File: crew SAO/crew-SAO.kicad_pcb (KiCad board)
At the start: 2 copper layers, 78.8 x 16.5 mm, 3 parts

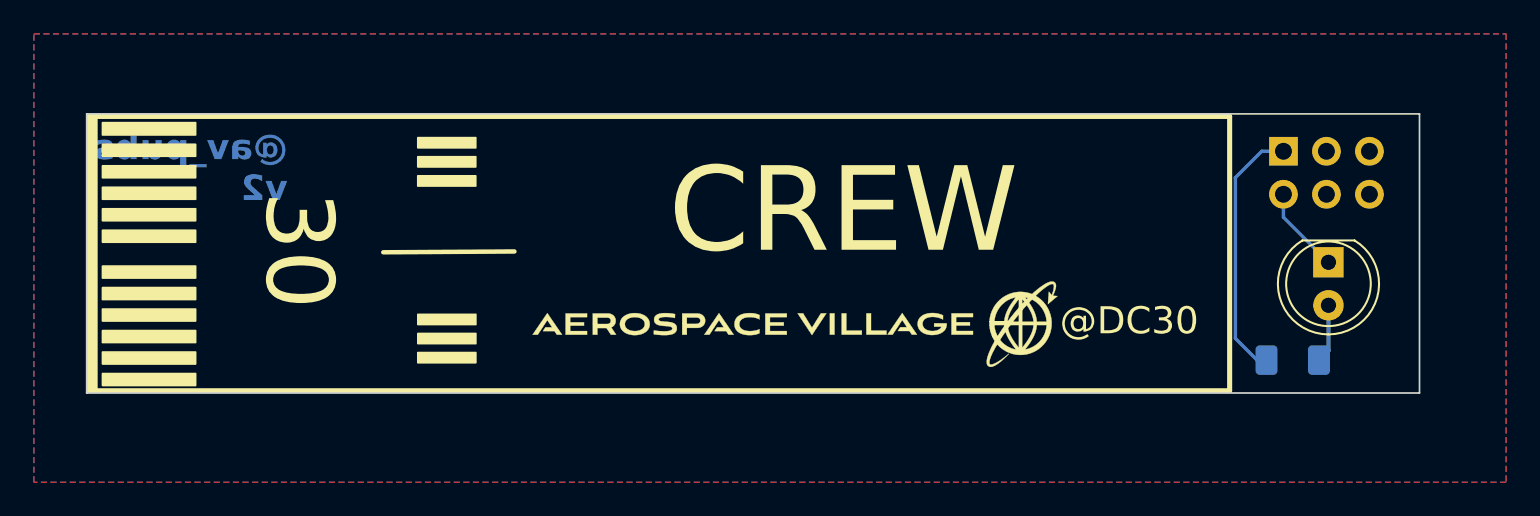
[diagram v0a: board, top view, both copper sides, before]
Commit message: speaker and crew SAOs updated to v3 that moves the connector slightly so it doesn't stick out
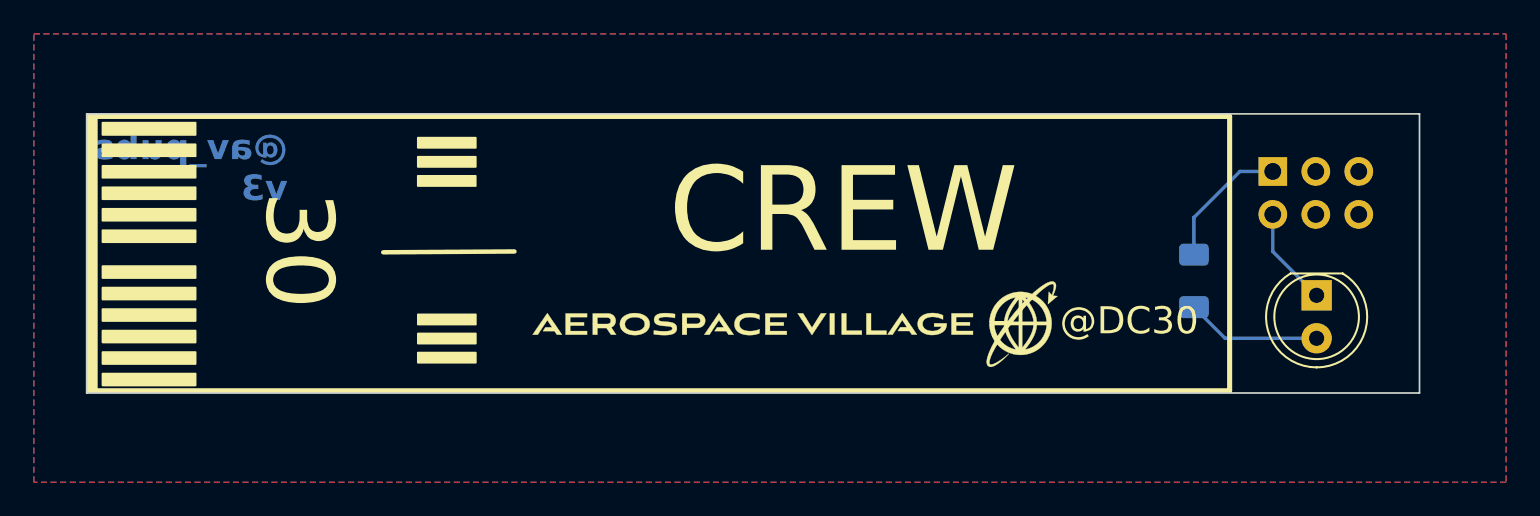
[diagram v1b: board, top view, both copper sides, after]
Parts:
- moved REF** 7.48 mm to (149.6, 132.6), turned to -90 degrees
- moved REF** 2.07 mm to (156.8, 133.4)
- moved REF** 1.35 mm to (154.2, 126.1)
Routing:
- net (no net): track 24.0 -> 21.9 mm
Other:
- board text added: "@av_pubs v3"
- board text removed: "@av_pubs v2"
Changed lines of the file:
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@@
   (net 0 "")
   (footprint "LED_THT:LED_D5.0mm" (layer "F.Cu")
-    (at 157.5 131.5 -90)
+    (at 156.8 133.45 -90)
     (descr "LED, diameter 5.0mm, 2 pins, http://cdn-reichelt.de/documents/datenblatt/A500/LL-504BC2E-009.pdf")
     (tags "LED diameter 5.0mm 2 pins")
@@
   )
   (footprint "Connector_PinHeader_2.54mm:PinHeader_2x03_P2.54mm_Vertical" (layer "B.Cu")
-    (at 154.84 124.94 -90)
+    (at 154.21 126.13 -90)
     (descr "Through hole straight pin header, 2x03, 2.54mm pitch, double rows")
     (tags "Through hole pin header THT 2x03 2.54mm double row")
@@
   )
   (footprint "Resistor_SMD:R_1206_3216Metric_Pad1.30x1.75mm_HandSolder" (layer "B.Cu")
-    (at 155.39 137.28 180)
+    (at 149.55 132.6 -90)
     (descr "Resistor SMD 1206 (3216 Metric), square (rectangular) end terminal, IPC_7351 nominal with elongated pad for handsoldering. (Body size source: IPC-SM-782 page 72, https://www.pcb-3d.com/wordpress/wp-content/uploads/ipc-sm-782a_amendment_1_and_2.pdf), generated with kicad-footprint-generator")
     (tags "resistor handsolder")
     (attr smd)
-    (fp_text reference "REF**" (at 0 1.82) (layer "B.SilkS") hide
+    (fp_text reference "REF**" (at 0 1.82 -270) (layer "B.SilkS") hide
         (effects (font (size 1 1) (thickness 0.15)) (justify mirror))
     )
-    (fp_text value "R_1206_3216Metric_Pad1.30x1.75mm_HandSolder" (at 0 -1.82) (layer "B.Fab")
+    (fp_text value "R_1206_3216Metric_Pad1.30x1.75mm_HandSolder" (at 0 -1.82 -270) (layer "B.Fab")
         (effects (font (size 1 1) (thickness 0.15)) (justify mirror))
     )
-    (fp_text user "${REFERENCE}" (at 0 0) (layer "B.Fab")
+    (fp_text user "${REFERENCE}" (at 0 0 -270) (layer "B.Fab")
         (effects (font (size 0.8 0.8) (thickness 0.12)) (justify mirror))
     )
@@
     (fp_line (start 1.6 0.8) (end 1.6 -0.8)
       (stroke (width 0.1) (type solid)) (layer "B.Fab"))
-    (pad "1" smd roundrect (at -1.55 0 180) (size 1.3 1.75) (layers "B.Cu" "B.Paste" "B.Mask") (roundrect_rratio 0.1923076923))
-    (pad "2" smd roundrect (at 1.55 0 180) (size 1.3 1.75) (layers "B.Cu" "B.Paste" "B.Mask") (roundrect_rratio 0.1923076923))
+    (pad "1" smd roundrect (at -1.55 0 270) (size 1.3 1.75) (layers "B.Cu" "B.Paste" "B.Mask") (roundrect_rratio 0.1923076923))
+    (pad "2" smd roundrect (at 1.55 0 270) (size 1.3 1.75) (layers "B.Cu" "B.Paste" "B.Mask") (roundrect_rratio 0.1923076923))
     (model "${KICAD6_3DMODEL_DIR}/Resistor_SMD.3dshapes/R_1206_3216Metric.wrl"
       (offset (xyz 0 0 0))
@@
   (gr_rect (start 84.12 122.73) (end 162.88 139.22)
     (stroke (width 0.1) (type default)) (fill none) (layer "Edge.Cuts"))
-  (gr_text "@av_pubs\nv2" (at 96 128) (layer "B.Cu")
+  (gr_text "@av_pubs\nv3" (at 96 128) (layer "B.Cu")
     (effects (font (size 1.5 1.5) (thickness 0.3) bold) (justify left bottom mirror))
   )
-  (gr_text "jlcjlcjlcjlc" (at 91 137.5) (layer "B.SilkS")
-    (effects (font (size 1.5 1.5) (thickness 0.3) bold) (justify mirror))
+  (gr_text "jlcjlcjlcjlc" (at 92.45 138.65) (layer "B.SilkS")
+    (effects (font (size 1 1) (thickness 0.15)) (justify left bottom mirror))
   )
   (gr_text "30" (at 94.3 127.29 -90) (layer "F.SilkS")
@@
     )
   )
-  (segment (start 152 126.5) (end 152 136) (width 0.2) (layer "B.Cu") (net 0))
-  (segment (start 153.28 137.28) (end 153.84 137.28) (width 0.2) (layer "B.Cu") (net 0))
-  (segment (start 157.5 134.04) (end 157.5 136.72) (width 0.25) (layer "B.Cu") (net 0))
-  (segment (start 154.84 124.94) (end 153.56 124.94) (width 0.2) (layer "B.Cu") (net 0))
-  (segment (start 154.84 127.48) (end 154.84 128.84) (width 0.2) (layer "B.Cu") (net 0))
-  (segment (start 153.56 124.94) (end 152 126.5) (width 0.2) (layer "B.Cu") (net 0))
-  (segment (start 154.84 128.84) (end 157.5 131.5) (width 0.2) (layer "B.Cu") (net 0))
-  (segment (start 152 136) (end 153.28 137.28) (width 0.2) (layer "B.Cu") (net 0))
-  (segment (start 157.5 136.72) (end 156.94 137.28) (width 0.25) (layer "B.Cu") (net 0))
+  (segment (start 156.8 135.99) (end 151.39 135.99) (width 0.2) (layer "B.Cu") (net 0))
+  (segment (start 149.55 131.05) (end 149.55 128.85) (width 0.2) (layer "B.Cu") (net 0))
+  (segment (start 149.55 128.85) (end 152.27 126.13) (width 0.2) (layer "B.Cu") (net 0))
+  (segment (start 154.21 128.67) (end 154.21 130.86) (width 0.2) (layer "B.Cu") (net 0))
+  (segment (start 151.39 135.99) (end 149.55 134.15) (width 0.2) (layer "B.Cu") (net 0))
+  (segment (start 154.21 130.86) (end 156.8 133.45) (width 0.2) (layer "B.Cu") (net 0))
+  (segment (start 152.27 126.13) (end 154.21 126.13) (width 0.2) (layer "B.Cu") (net 0))
   (zone (net 0) (net_name "") (layers F&B.Cu) (hatch edge 0.508)
     (connect_pads (clearance 0.508))
